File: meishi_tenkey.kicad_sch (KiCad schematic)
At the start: 45 parts, among them J1 Conn_01x07_Socket, J2 Conn_01x07_Socket, J3 Conn_01x07_Pin, J4 Conn_01x07_Pin, SW1 SW_Push, SW10 SW_Push, SW11 SW_Push, SW12 SW_Push, SW13 SW_Push, SW14 SW_Push, SW15 SW_Push, SW16 SW_Push, SW17 SW_Push, SW18 SW_Push, SW19 SW_Push, SW2 SW_Push, SW20 SW_Push, SW3 SW_Push, SW4 SW_Push, SW5 SW_Push, SW6 SW_Push, SW7 SW_Push, SW8 SW_Push, SW9 SW_Push, U1 XIAO-RP2040-SMD

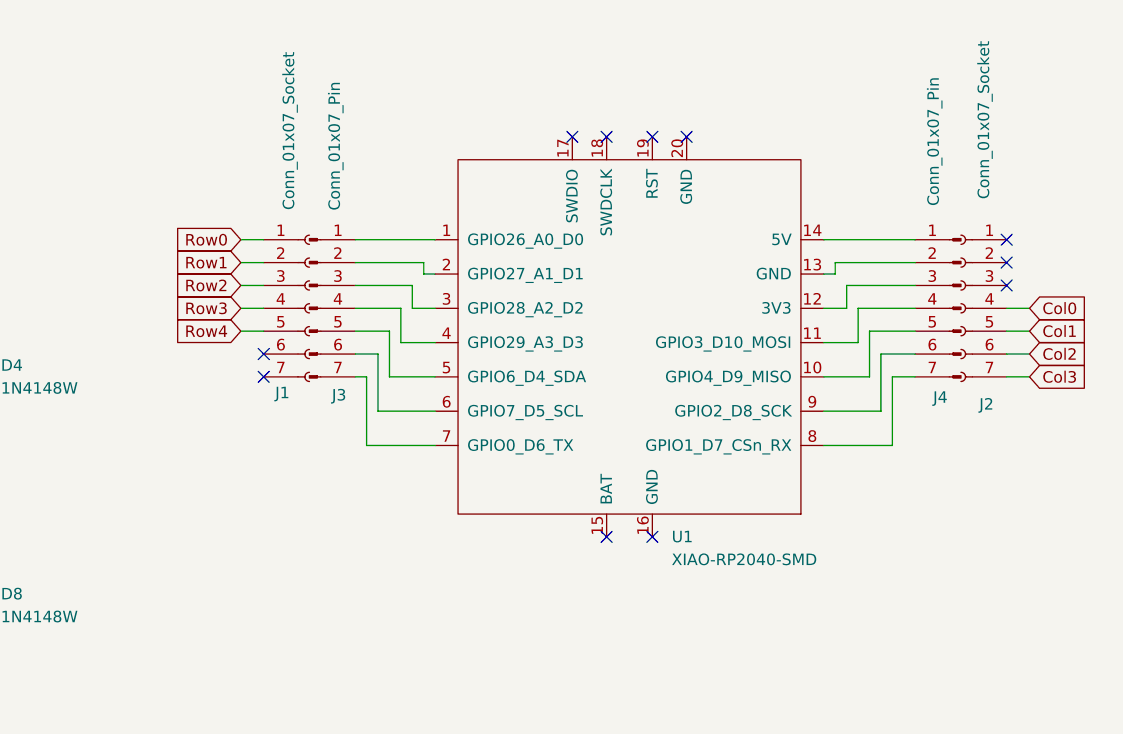
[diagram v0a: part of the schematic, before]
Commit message: fix: correct MCU through-hole pitch in footprint (v0.2)
Fix incorrect through-hole spacing for the microcontroller footprint.
Regenerate all gerber files with the corrected PCB design.
Update README to note the fix for v0.1 users.

Co-Authored-By: Claude Opus 4.6 <noreply@anthropic.com>
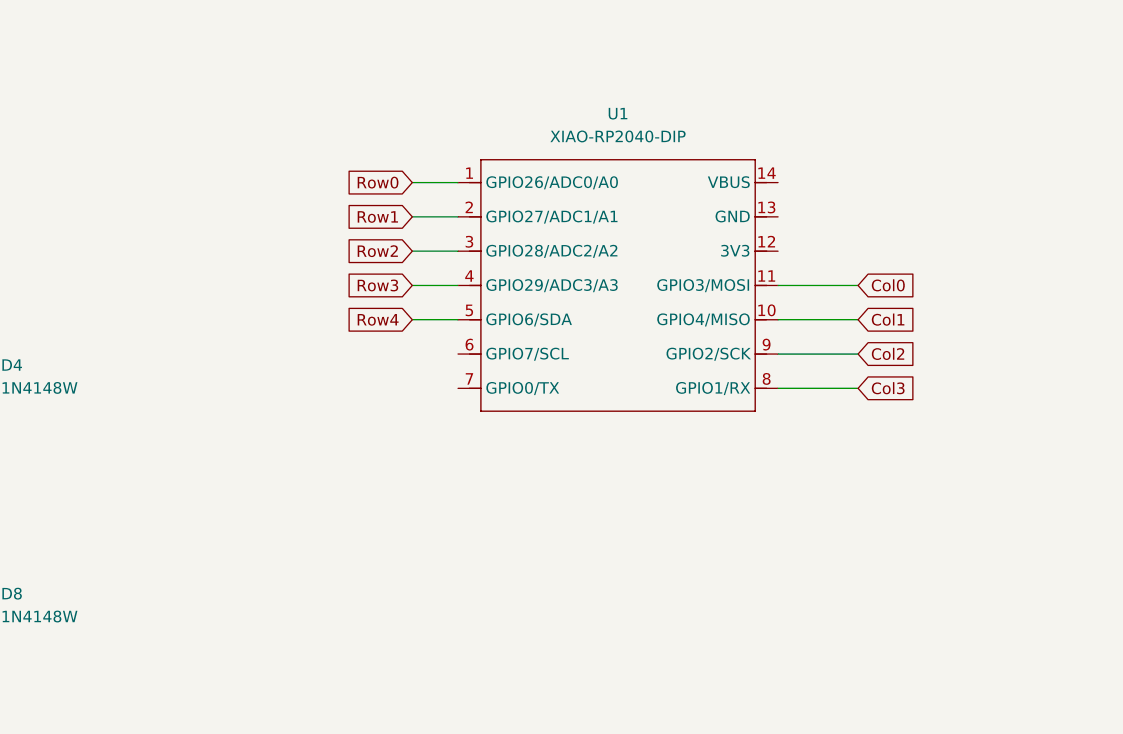
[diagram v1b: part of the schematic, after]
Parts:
- removed J1, J2: Conn_01x07_Socket, Connector_PinSocket_2.54mm:PinSocket_1x07_P2.54mm_Vertical, symbol Connector:Conn_01x07_Socket
- removed J3, J4: Conn_01x07_Pin, Connector_PinHeader_2.54mm:PinHeader_1x07_P2.54mm_Vertical, symbol Connector:Conn_01x07_Pin
- removed U1: XIAO-RP2040-SMD, Seeed Studio XIAO Series Library:XIAO-RP2040-SMD, symbol Xiao:XIAO-RP2040-SMD
- added U1: XIAO-RP2040-DIP, Seeed Studio XIAO Series Library:XIAO-RP2040-DIP, symbol Xiao:XIAO-RP2040-DIP
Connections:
- net Col0: now also U1.11 (GPIO3/MOSI)
- net Col1: now also U1.10 (GPIO4/MISO)
- net Col2: now also U1.9 (GPIO2/SCK)
- net Col3: now also U1.8 (GPIO1/RX)
- net Row0: now also U1.1 (GPIO26/ADC0/A0)
- net Row1: now also U1.2 (GPIO27/ADC1/A1)
- net Row2: now also U1.3 (GPIO28/ADC2/A2)
- net Row3: now also U1.4 (GPIO29/ADC3/A3)
- net Row4: now also U1.5 (GPIO6/SDA)
- no-connect marks 11 -> 0
